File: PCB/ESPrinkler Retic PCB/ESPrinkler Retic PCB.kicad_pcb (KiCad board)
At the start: 2 copper layers, 120.4 x 85.7 mm, 158 parts, among them J4 Conn_01x19, J5 Conn_01x19, J6 Conn_01x04, Q1 AO3400A, Q10 AO3400A, Q11 AO3400A, Q2 AO3400A, Q3 AO3400A, Q4 AO3400A, Q5 AO3400A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

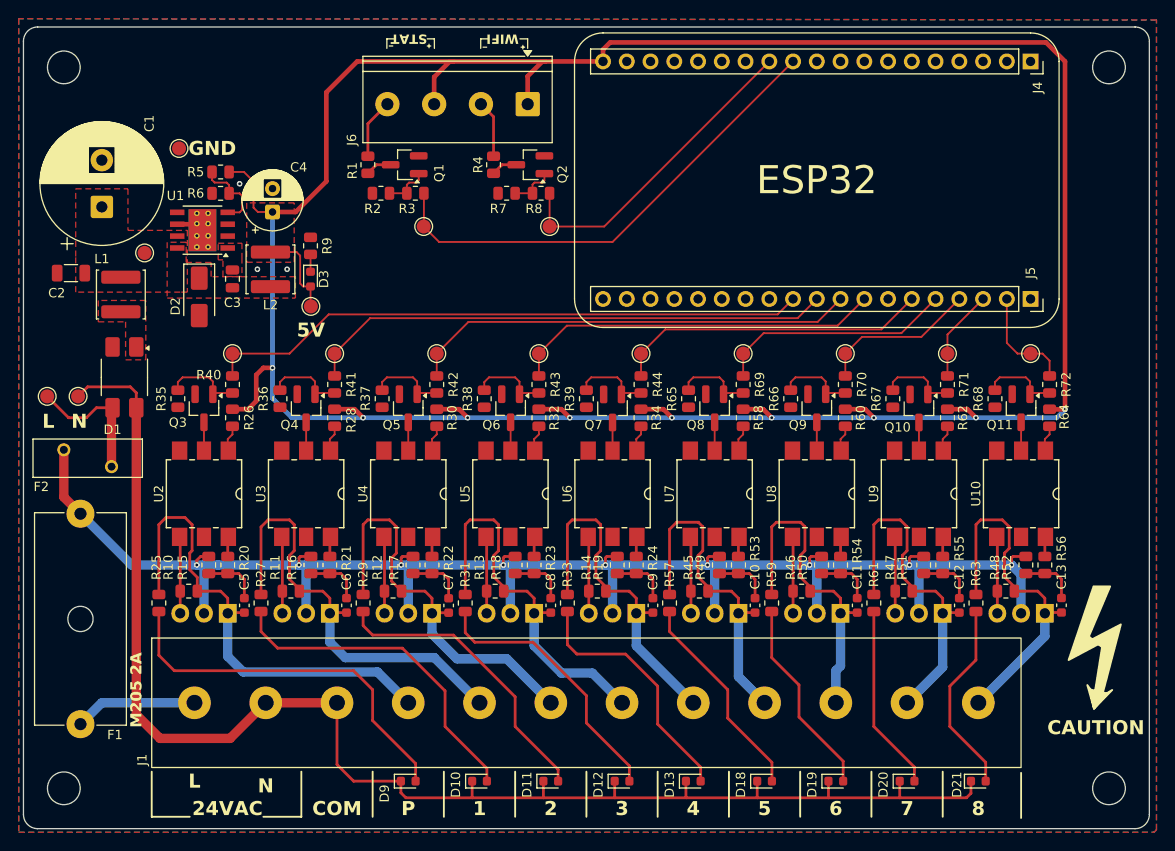
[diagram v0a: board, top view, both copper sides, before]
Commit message: Remove snubber and bring Kicad V10 update
Remove snubber from triac driver as its not required.

Attempt to start migrating to Kicad V10
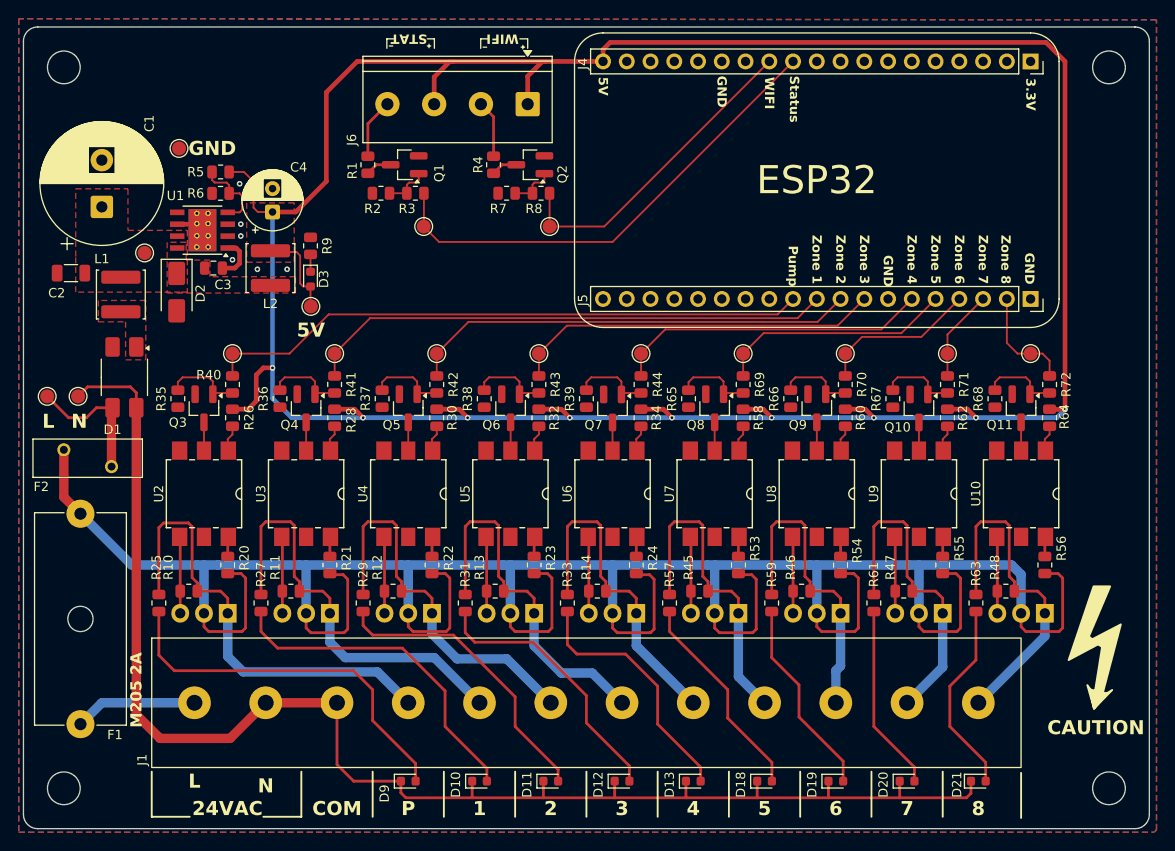
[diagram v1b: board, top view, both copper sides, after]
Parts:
- removed C10, C11, C12, C13, C5, C6, C7, C8, C9: 2.2nF, Capacitor_SMD:C_0603_1608Metric
- removed R15, R16, R17, R18, R19, R49, R50, R51, R52: 300R, Resistor_SMD:R_0805_2012Metric
- moved D2 2.47 mm to (148.7, 92.7)
- moved C3 2.33 mm to (152.7, 90.2), turned to 180 degrees
- moved L2 0.14 mm to (158.7, 90.2)
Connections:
- R20 pad 1: Net-(C5-Pad1) -> LIVE_SOLENOID
- R21 pad 1: Net-(C6-Pad1) -> LIVE_SOLENOID
- R22 pad 1: Net-(C7-Pad1) -> LIVE_SOLENOID
- R23 pad 1: Net-(C8-Pad1) -> LIVE_SOLENOID
- R24 pad 1: Net-(C9-Pad1) -> LIVE_SOLENOID
- R53 pad 1: Net-(C10-Pad1) -> LIVE_SOLENOID
- R54 pad 1: Net-(C11-Pad1) -> LIVE_SOLENOID
- R55 pad 1: Net-(C12-Pad1) -> LIVE_SOLENOID
- R56 pad 1: Net-(C13-Pad1) -> LIVE_SOLENOID
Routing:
- net LIVE_SOLENOID: track 175.5 -> 279.5 mm, vias 9 -> 0
- net Net-(C7-Pad1): track 6.10 -> 0.00 mm
- net Net-(C5-Pad1): track 6.08 -> 0.00 mm
- net Net-(C9-Pad1): track 6.08 -> 0.00 mm
- net Net-(C8-Pad1): track 6.08 -> 0.00 mm
- net Net-(C12-Pad1): track 6.08 -> 0.00 mm
- net Net-(C11-Pad1): track 6.08 -> 0.00 mm
- net Net-(C10-Pad1): track 6.08 -> 0.00 mm
- net Net-(C6-Pad1): track 6.08 -> 0.00 mm
- net Net-(C13-Pad1): track 6.07 -> 0.00 mm
- net Net-(U1-BOOT): track 0.00 -> 4.75 mm
- net /Power & IO/To Zone 4: track 38.3 -> 35.6 mm
- net /Power & IO/To Zone 3: track 41.6 -> 38.9 mm
- net /Power & IO/To Pump: track 52.2 -> 49.5 mm
- net /Power & IO/To Zone 8: track 38.6 -> 36.0 mm
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- removed copper zone on F.Cu, net Net-(U1-BOOT)
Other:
- board text added: "3.3V"
- board text added: "Pump"
- board text added: "Status"
- board text added: "Zone 1"
- board text added: "Zone 2"
- board text added: "Zone 3"
- board text added: "Zone 4"
- board text added: "Zone 5"
- board text added: "Zone 6"
- board text added: "Zone 7"
- board text added: "Zone 8"

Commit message: Change DC-DC converter & PCB routing
Previous DC-DC converter max input voltage was close to VIN. Changed out for 40V rated input, and a simpler design.

Also re-routed 5V rail to top layer to reduce layer swapping using vias for power lines
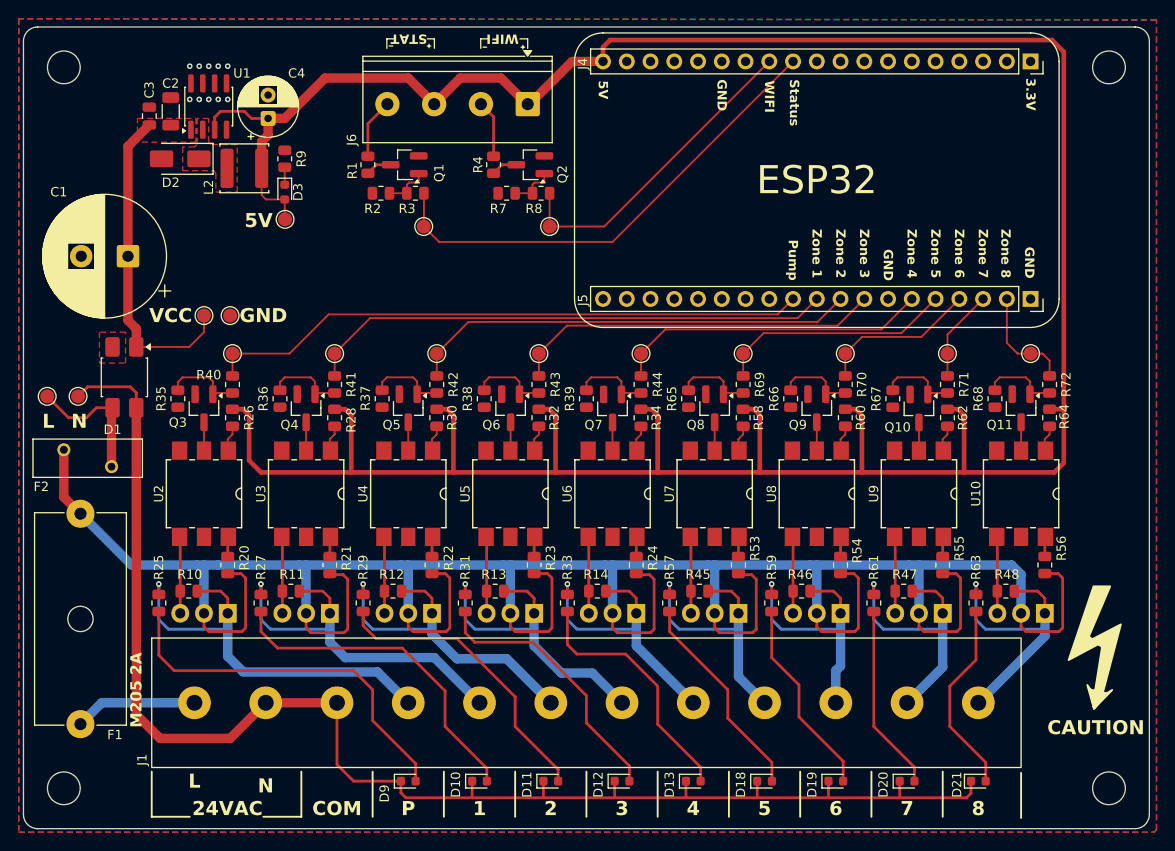
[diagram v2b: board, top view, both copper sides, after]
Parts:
- removed L1: 33uH, Inductor_SMD:L_APV_ANR5045
- removed R5: 10k, Resistor_SMD:R_0805_2012Metric
- removed R6: 3.24k, Resistor_SMD:R_0805_2012Metric
- C3: value 10nF -> 100nF
- L2: value 33uH -> 68uH
- U1: value TPS5430DDA -> XL1509-5.0; footprint Package_SO:TI_SO-PowerPAD-8_ThermalVias -> Package_SO:SOIC-8_3.9x4.9mm_P1.27mm
- moved C2 20.3 mm to (148.1, 73.4), turned to 90 degrees
- moved TP3 18.7 mm to (154.4, 95.2)
- moved C3 17.6 mm to (145.8, 73.9), turned to -90 degrees
- moved D2 14.3 mm to (149.1, 78.5), turned to 180 degrees
- moved U1 13.2 mm to (152.1, 72.9), turned to 90 degrees
- moved L2 11.0 mm to (156.0, 79.5), turned to 0 degrees
- moved C4 10.0 mm to (158.5, 74.2)
- moved D3 9.71 mm to (160.3, 82.0)
- moved R9 9.71 mm to (160.3, 78.5)
- moved TP6 9.71 mm to (160.3, 85.0)
- moved TP4 9.23 mm to (151.6, 95.2)
- moved C1 5.97 mm to (143.5, 88.9), turned to 180 degrees
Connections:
- C3 pad 1: Net-(U1-BOOT) -> GND
- C3 pad 2: Net-(D2-K) -> VCC
- D1 pad 1: Net-(D1-+) -> VCC
- U1 pad 1: Net-(U1-BOOT) -> VCC
- U1 pad 2: unconnected-(U1-NC-Pad2) -> Net-(D2-K)
- U1 pad 3: unconnected-(U1-NC-Pad3) -> +5V
- U1 pad 4: Net-(U1-VSENSE) -> unconnected-(U1-~{EN}-Pad4)
- U1 pad 5: unconnected-(U1-EN-Pad5) -> GND
- U1 pad 7: VCC -> GND
- U1 pad 8: Net-(D2-K) -> GND
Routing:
- net VCC: track 0.00 -> 34.7 mm
- net Net-(U1-VSENSE): track 8.42 -> 0.00 mm
- net +5V: track 305.6 -> 313.0 mm, vias 9 -> 0
- net /Power & IO/To Zone 7: track 34.7 -> 29.0 mm, vias 0 -> 1
- net /Power & IO/To Zone 8: track 36.0 -> 30.4 mm, vias 0 -> 1
- net /Power & IO/To Zone 6: track 33.3 -> 27.7 mm, vias 0 -> 1
- net /Power & IO/To Zone 3: track 38.9 -> 33.3 mm, vias 0 -> 1
- net /Power & IO/To Zone 2: track 41.5 -> 35.8 mm, vias 0 -> 1
- net /Power & IO/To Zone 1: track 45.3 -> 39.7 mm, vias 0 -> 1
- net /Power & IO/To Pump: track 49.5 -> 43.9 mm, vias 0 -> 1
- net /Power & IO/To Zone 5: track 34.3 -> 28.6 mm, vias 0 -> 1
- net /Power & IO/To Zone 4: track 35.6 -> 30.0 mm, vias 0 -> 1
- net Net-(U1-BOOT): track 4.75 -> 0.00 mm
- net GND: track 3.81 -> 0.00 mm, vias 6 -> 10
- removed copper zone on F.Cu, net +5V
- removed copper zone on F.Cu, net Net-(D1-+)
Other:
- board text added: "VCC"

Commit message: Add TVS protection
Added SMAJ33A TVS on VCC
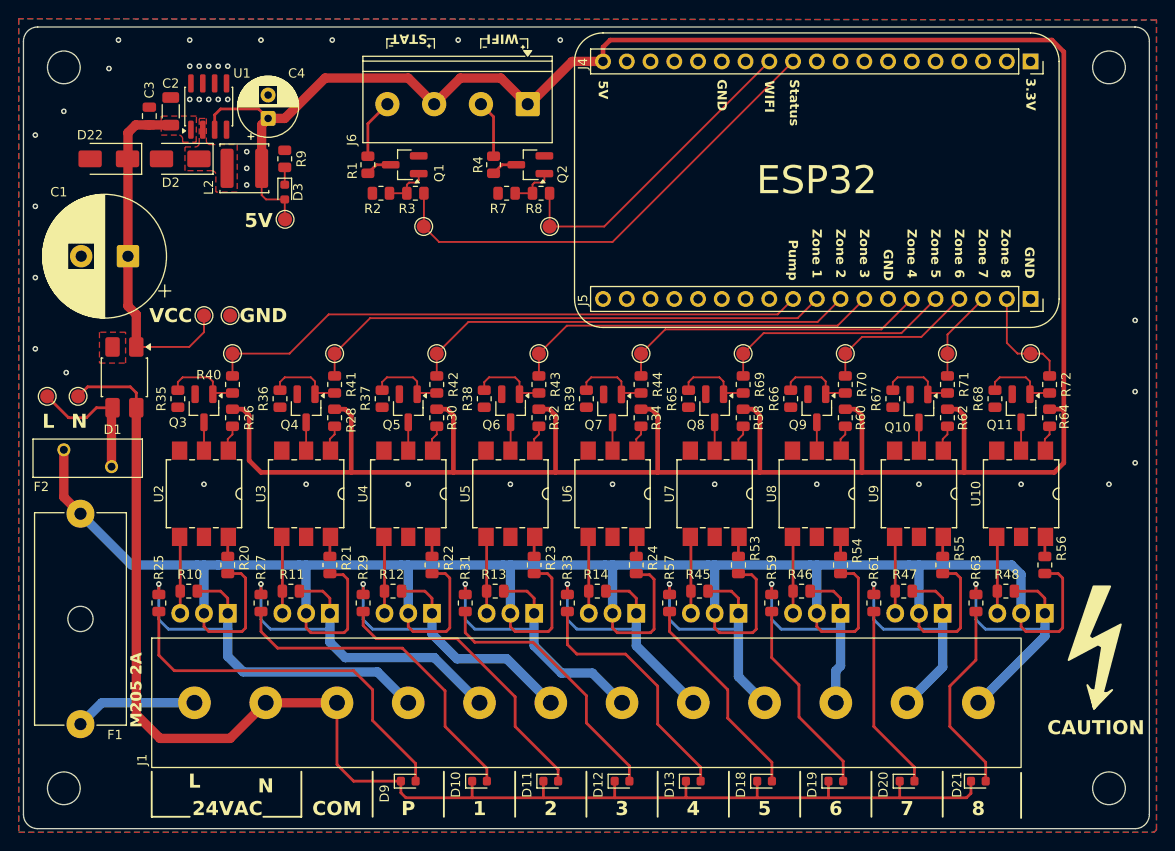
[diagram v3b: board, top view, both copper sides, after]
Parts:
- added D22: SMAJ33A, Diode_SMD:D_SMA, F.Cu at (141.5, 78.5)
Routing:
- net VCC: track 34.7 -> 37.9 mm
- net GND: vias 10 -> 39

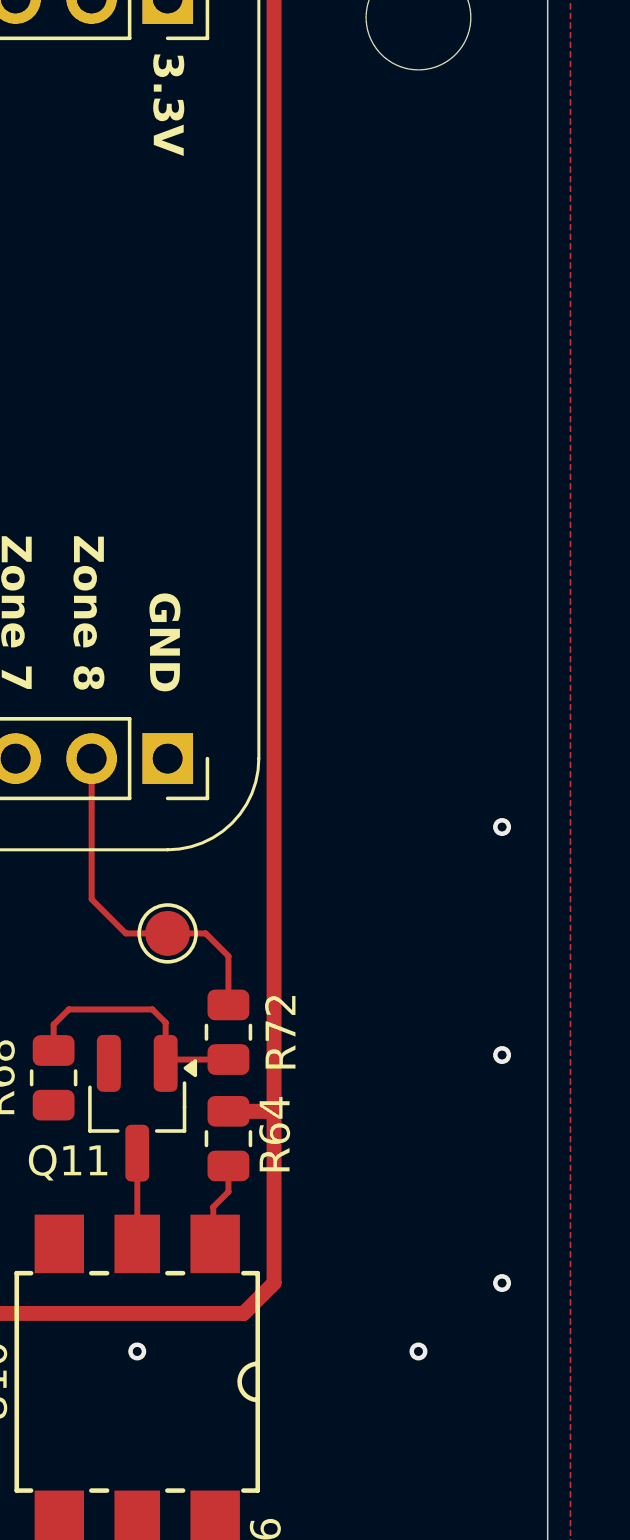
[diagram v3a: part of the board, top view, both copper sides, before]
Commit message: Start updating models
Updating models since moving to kicad 10.

Will begin migrating to project library entirely
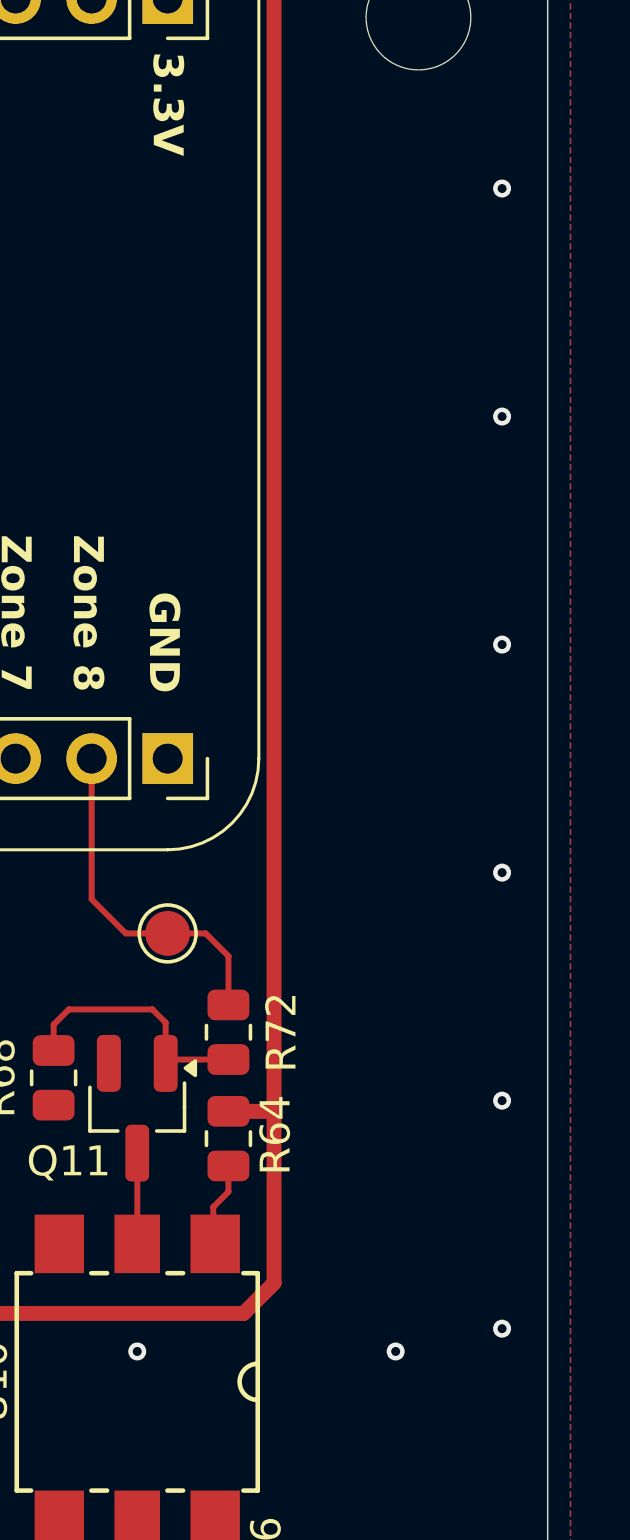
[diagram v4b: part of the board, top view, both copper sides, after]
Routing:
- net GND: vias 39 -> 42
